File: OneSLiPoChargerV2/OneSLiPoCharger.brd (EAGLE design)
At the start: 86.4 x 52.1 mm, 55 parts, among them IC1 LM358N

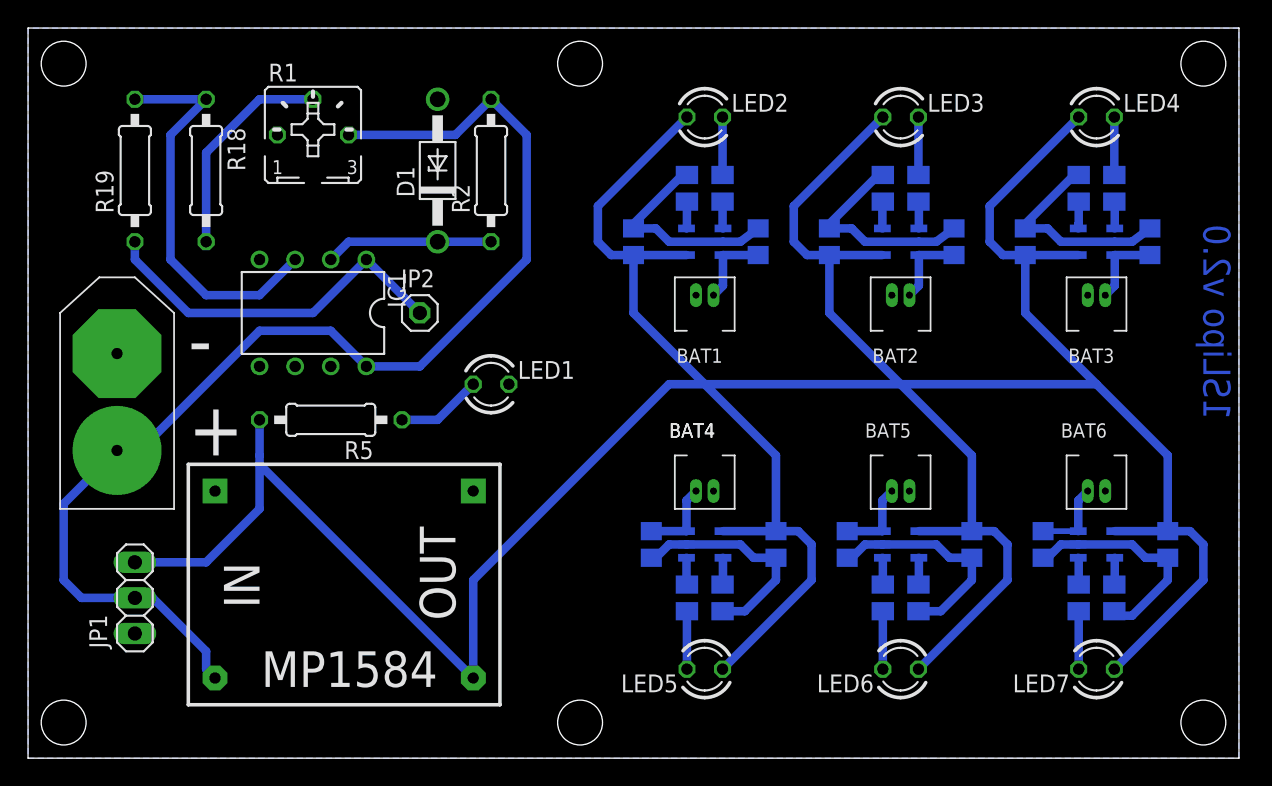
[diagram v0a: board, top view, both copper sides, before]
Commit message: Add a voltage divider on opamp output to drop voltage for the mp1584 enable pin.
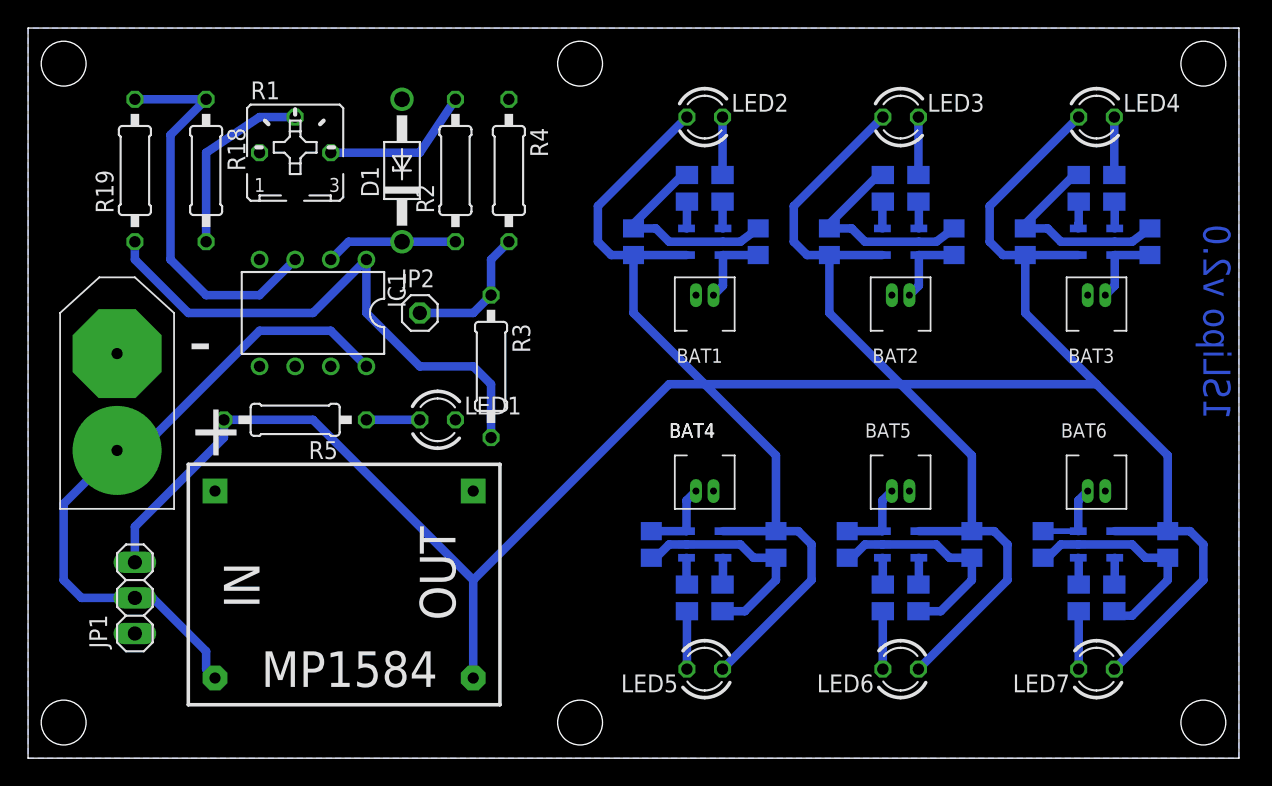
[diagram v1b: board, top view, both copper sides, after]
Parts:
- added R3: 4.7K, rcl:0207/10
- added R4: 1K, rcl:0207/10
- moved LED1 4.58 mm to (29.2, 24.1)
- moved R2 2.54 mm to (30.5, 41.9)
- moved D1 2.54 mm to (26.7, 41.9)
- moved R5 2.54 mm to (19.1, 24.1)
- moved R1 1.80 mm to (19.1, 43.2)
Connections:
- new net N$2: JP2.1, R3.1, R4.2
- net GND: now also R4.1
- net N$4: now also R3.2; no longer JP2.1
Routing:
- net VCC: track 85.9 -> 58.6 mm
- net N$4: track 26.3 -> 39.6 mm
- net N$2: track 0.00 -> 9.94 mm
- net +5V: track 276.7 -> 273.6 mm
- net N$3: track 12.0 -> 9.42 mm
- net N$10: track 6.13 -> 3.81 mm
- net N$1: track 15.5 -> 13.5 mm
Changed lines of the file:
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@@
 <attribute name="NAME" x="54.61" y="39.37" size="1.27" layer="26" rot="MR270"/>
 </element>
-<element name="D1" library="diode" package="DO41Z10" value="1N4728" x="29.21" y="41.91" smashed="yes" rot="R90">
-<attribute name="NAME" x="27.559" y="40.005" size="1.27" layer="25" ratio="10" rot="R90"/>
+<element name="D1" library="diode" package="DO41Z10" value="1N4728" x="26.67" y="41.91" smashed="yes" rot="R90">
+<attribute name="NAME" x="25.019" y="40.005" size="1.27" layer="25" ratio="10" rot="R90"/>
 </element>
 <element name="IC1" library="linear" package="DIL08" value="LM358N" x="20.32" y="31.75" rot="R180"/>
-<element name="LED1" library="led" package="LED3MM" value="" x="33.02" y="26.67"/>
+<element name="LED1" library="led" package="LED3MM" value="" x="29.21" y="24.13"/>
 <element name="LED2" library="led" package="LED3MM" value="" x="48.26" y="45.72"/>
-<element name="R1" library="pot" package="B25P" value="" x="20.32" y="44.45"/>
-<element name="R2" library="rcl" package="0207/10" value="1K" x="33.02" y="41.91" rot="R90"/>
+<element name="R1" library="pot" package="B25P" value="" x="19.05" y="43.18"/>
+<element name="R2" library="rcl" package="0207/10" value="1K" x="30.48" y="41.91" rot="R90"/>
 <element name="R6" library="rcl" package="M0805" value="" x="49.53" y="40.64" smashed="yes" rot="MR90">
 <attribute name="NAME" x="50.8" y="39.37" size="1.27" layer="26" rot="MR90"/>
@@
 <attribute name="NAME" x="45.72" y="41.91" size="1.27" layer="26" rot="MR270"/>
 </element>
-<element name="R5" library="rcl" package="0207/10" value="4.7K" x="21.59" y="24.13" rot="R180"/>
+<element name="R5" library="rcl" package="0207/10" value="4.7K" x="19.05" y="24.13" rot="R180"/>
 <element name="U$1" library="MCP73831" package="MCP73831-SOT23" value="MCP73831" x="48.26" y="36.83" rot="MR270"/>
 <element name="U$2" library="Picoblade" package="PICOBLADE-2PIN" value="PICOBLADE-2PIN" x="48.26" y="33.02"/>
@@
 <element name="U$14" library="VRegModules" package="MP1584MOD-TH" value="MP1584EN-MOD" x="31.75" y="19.05" rot="R180"/>
 <element name="JP2" library="pinhead" package="1X01" value="" x="27.94" y="31.75"/>
+<element name="R3" library="rcl" package="0207/10" value="4.7K" x="33.02" y="27.94" rot="R270"/>
+<element name="R4" library="rcl" package="0207/10" value="1K" x="34.29" y="41.91" rot="R270"/>
 </elements>
 <signals>
@@
 <contactref element="IC1" pad="2"/>
 <wire x1="21.59" y1="35.56" x2="22.86" y2="36.83" width="0.6096" layer="16"/>
-<wire x1="22.86" y1="36.83" x2="29.21" y2="36.83" width="0.6096" layer="16"/>
-<wire x1="29.21" y1="36.83" x2="33.02" y2="36.83" width="0.6096" layer="16"/>
+<wire x1="22.86" y1="36.83" x2="26.67" y2="36.83" width="0.6096" layer="16"/>
+<wire x1="26.67" y1="36.83" x2="30.48" y2="36.83" width="0.6096" layer="16"/>
 </signal>
 <signal name="VCC">
@@
 <contactref element="JP1" pad="2"/>
 <contactref element="U$14" pad="IPOS"/>
-<wire x1="22.86" y1="44.45" x2="30.48" y2="44.45" width="0.6096" layer="16"/>
-<wire x1="30.48" y1="44.45" x2="33.02" y2="46.99" width="0.6096" layer="16"/>
-<wire x1="24.13" y1="27.94" x2="27.94" y2="27.94" width="0.6096" layer="16"/>
-<wire x1="27.94" y1="27.94" x2="35.56" y2="35.56" width="0.6096" layer="16"/>
-<wire x1="35.56" y1="35.56" x2="35.56" y2="44.45" width="0.6096" layer="16"/>
-<wire x1="35.56" y1="44.45" x2="33.02" y2="46.99" width="0.6096" layer="16"/>
+<wire x1="21.59" y1="43.18" x2="27.94" y2="43.18" width="0.6096" layer="16"/>
+<wire x1="27.94" y1="43.18" x2="30.48" y2="46.99" width="0.6096" layer="16"/>
 <wire x1="7.62" y1="11.43" x2="3.81" y2="11.43" width="0.6096" layer="16"/>
 <wire x1="3.81" y1="11.43" x2="2.54" y2="12.7" width="0.6096" layer="16"/>
@@
 <wire x1="12.7" y1="7.62" x2="12.7" y2="6.35" width="0.6096" layer="16"/>
 <wire x1="12.7" y1="6.35" x2="13.335" y2="5.715" width="0.6096" layer="16"/>
+<wire x1="21.59" y1="30.48" x2="21.59" y2="43.18" width="0" layer="19" extent="16-16"/>
 </signal>
 <signal name="GND">
@@
 <contactref element="U$14" pad="INEG"/>
 <contactref element="U$14" pad="ONEG"/>
+<contactref element="R4" pad="1"/>
 </signal>
 <signal name="N$4">
 <contactref element="IC1" pad="1"/>
 <contactref element="R19" pad="1"/>
-<contactref element="JP2" pad="1"/>
 <wire x1="20.32" y1="31.75" x2="24.13" y2="35.56" width="0.6096" layer="16"/>
-<wire x1="27.94" y1="31.75" x2="24.13" y2="35.56" width="0.6096" layer="16"/>
 <wire x1="7.62" y1="36.83" x2="7.62" y2="35.56" width="0.6096" layer="16"/>
 <wire x1="7.62" y1="35.56" x2="11.43" y2="31.75" width="0.6096" layer="16"/>
 <wire x1="11.43" y1="31.75" x2="20.32" y2="31.75" width="0.6096" layer="16"/>
+<contactref element="R3" pad="2"/>
+<wire x1="24.13" y1="35.56" x2="24.13" y2="31.75" width="0.6096" layer="16"/>
+<wire x1="24.13" y1="31.75" x2="27.94" y2="27.94" width="0.6096" layer="16"/>
+<wire x1="27.94" y1="27.94" x2="31.75" y2="27.94" width="0.6096" layer="16"/>
+<wire x1="31.75" y1="27.94" x2="33.02" y2="26.67" width="0.6096" layer="16"/>
+<wire x1="33.02" y1="26.67" x2="33.02" y2="22.86" width="0.6096" layer="16"/>
 </signal>
 <signal name="+5V">
@@
 <contactref element="JP1" pad="1"/>
 <contactref element="U$14" pad="OPOS"/>
-<wire x1="16.51" y1="24.13" x2="16.51" y2="21.59" width="0.6096" layer="16"/>
-<wire x1="16.51" y1="21.59" x2="16.51" y2="20.955" width="0.6096" layer="16"/>
-<wire x1="16.51" y1="20.955" x2="31.75" y2="5.715" width="0.6096" layer="16"/>
 <wire x1="31.75" y1="5.715" x2="31.75" y2="12.7" width="0.6096" layer="16"/>
 <wire x1="31.75" y1="12.7" x2="45.72" y2="26.67" width="0.6096" layer="16"/>
-<wire x1="7.62" y1="13.97" x2="12.7" y2="13.97" width="0.6096" layer="16"/>
-<wire x1="12.7" y1="13.97" x2="16.51" y2="17.78" width="0.6096" layer="16"/>
-<wire x1="16.51" y1="17.78" x2="16.51" y2="20.955" width="0.6096" layer="16"/>
+<wire x1="7.62" y1="13.97" x2="7.62" y2="16.51" width="0.6096" layer="16"/>
+<wire x1="7.62" y1="16.51" x2="13.97" y2="22.86" width="0.6096" layer="16"/>
+<wire x1="13.97" y1="22.86" x2="13.97" y2="24.13" width="0.6096" layer="16"/>
+<wire x1="13.97" y1="24.13" x2="20.32" y2="24.13" width="0.6096" layer="16"/>
+<wire x1="20.32" y1="24.13" x2="31.75" y2="12.7" width="0.6096" layer="16"/>
 </signal>
 <signal name="N$10">
 <contactref element="R5" pad="1"/>
 <contactref element="LED1" pad="A"/>
-<wire x1="26.67" y1="24.13" x2="29.21" y2="24.13" width="0.6096" layer="16"/>
-<wire x1="29.21" y1="24.13" x2="31.75" y2="26.67" width="0.6096" layer="16"/>
+<wire x1="24.13" y1="24.13" x2="27.94" y2="24.13" width="0.6096" layer="16"/>
 </signal>
 <signal name="N$6">
@@
 <contactref element="R18" pad="2"/>
 <wire x1="12.7" y1="36.83" x2="12.7" y2="43.18" width="0.6096" layer="16"/>
-<wire x1="12.7" y1="43.18" x2="16.51" y2="46.99" width="0.6096" layer="16"/>
-<wire x1="16.51" y1="46.99" x2="20.32" y2="46.99" width="0.6096" layer="16"/>
+<wire x1="12.7" y1="43.18" x2="16.51" y2="45.72" width="0.6096" layer="16"/>
+<wire x1="16.51" y1="45.72" x2="19.05" y2="45.72" width="0.6096" layer="16"/>
 </signal>
 <signal name="N$31">
@@
 <wire x1="10.16" y1="35.56" x2="12.7" y2="33.02" width="0.6096" layer="16"/>
 </signal>
+<signal name="N$2">
+<contactref element="R3" pad="1"/>
+<contactref element="R4" pad="2"/>
+<contactref element="JP2" pad="1"/>
+<wire x1="27.94" y1="31.75" x2="31.75" y2="31.75" width="0.6096" layer="16"/>
+<wire x1="31.75" y1="31.75" x2="33.02" y2="33.02" width="0.6096" layer="16"/>
+<wire x1="33.02" y1="33.02" x2="33.02" y2="35.56" width="0.6096" layer="16"/>
+<wire x1="33.02" y1="35.56" x2="34.29" y2="36.83" width="0.6096" layer="16"/>
+</signal>
 </signals>

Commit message: Clean up addition of the buck module.
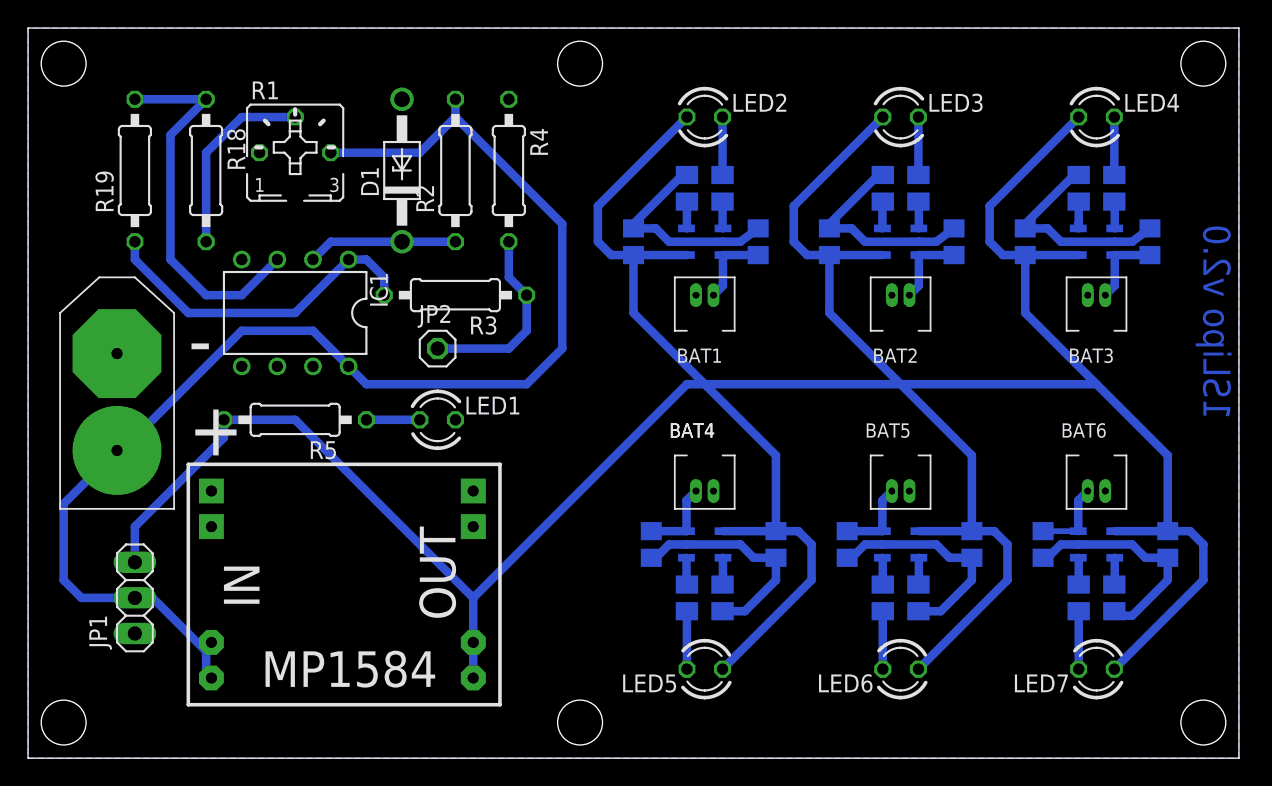
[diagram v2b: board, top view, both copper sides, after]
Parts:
- moved R3 5.68 mm to (30.5, 33.0), turned to 180 degrees
- moved JP2 2.84 mm to (29.2, 29.2)
- moved IC1 1.27 mm to (19.1, 31.8)
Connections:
- net +5V: now also U$14.OPOS1
- net GND: now also U$14.INEG1, U$14.ONEG1
- net VCC: now also U$14.IPOS1
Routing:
- net VCC: track 58.6 -> 94.7 mm
- net N$4: track 39.6 -> 24.0 mm
- net N$2: track 9.94 -> 13.8 mm
- net N$31: track 28.6 -> 27.3 mm
- net N$3: track 9.42 -> 10.7 mm
